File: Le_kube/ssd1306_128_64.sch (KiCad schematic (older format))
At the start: 15 parts

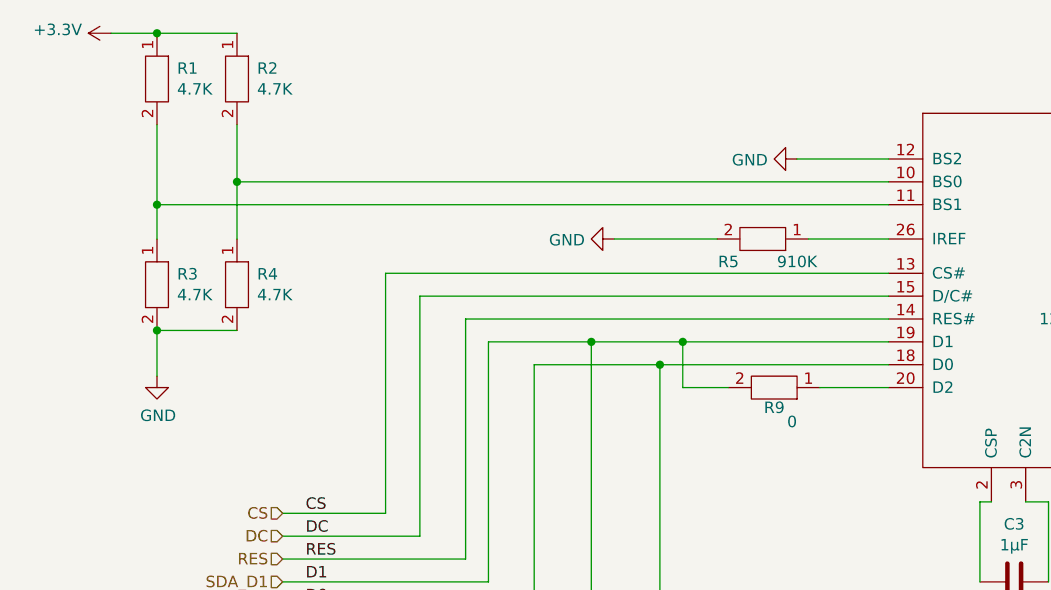
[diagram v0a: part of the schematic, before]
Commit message: merge screen + temp sensor CAO
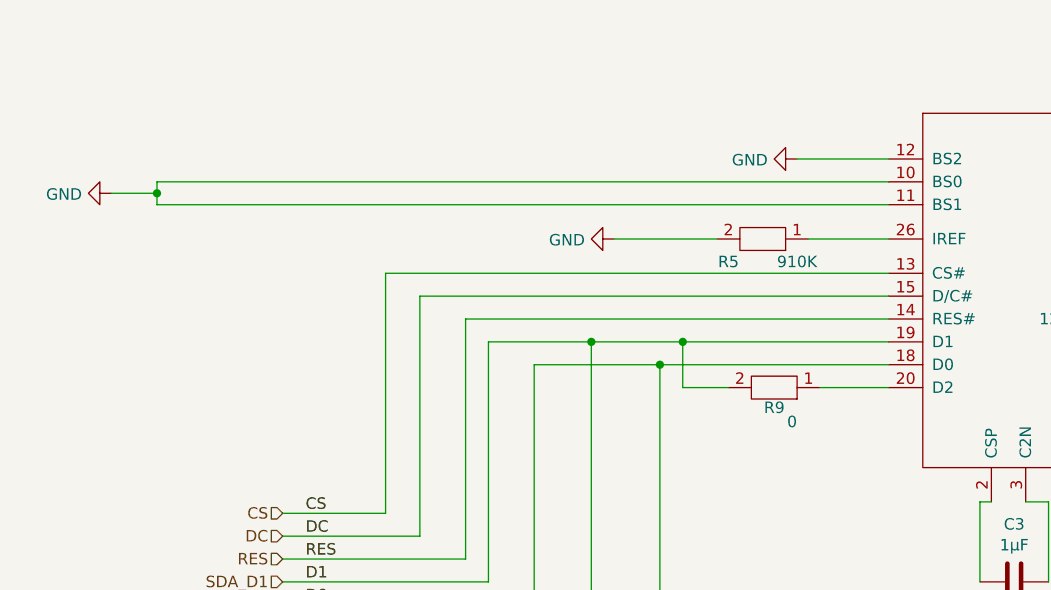
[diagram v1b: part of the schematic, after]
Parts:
- removed R1, R2, R3, R4: 4.7K, symbol Kube_library:R
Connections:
- net GND: now also U.10 (BS0), U.11 (BS1)
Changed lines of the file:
@@
 Comment4 ""
 $EndDescr
-$Comp
-L Kube_library:R R1
-U 1 1 606D3DEF
-P 2400 1350
-F 0 "R1" V 2354 1438 50  0000 L CNN
-F 1 "4.7K" V 2445 1438 50  0000 L CNN
-F 2 "" H 2400 1350 50  0001 C CNN
-F 3 "" H 2400 1350 50  0001 C CNN
-	1    2400 1350
-	0    1    1    0
-$EndComp
-$Comp
-L Kube_library:R R2
-U 1 1 606D4491
-P 2750 1350
-F 0 "R2" V 2704 1438 50  0000 L CNN
-F 1 "4.7K" V 2795 1438 50  0000 L CNN
-F 2 "" H 2750 1350 50  0001 C CNN
-F 3 "" H 2750 1350 50  0001 C CNN
-	1    2750 1350
-	0    1    1    0
-$EndComp
-Wire Wire Line
-	2750 1150 2400 1150
-Connection ~ 2400 1150
-Wire Wire Line
-	2400 1150 2200 1150
-$Comp
-L Kube_library:R R4
-U 1 1 606D4D1A
-P 2750 2250
-F 0 "R4" V 2704 2338 50  0000 L CNN
-F 1 "4.7K" V 2795 2338 50  0000 L CNN
-F 2 "" H 2750 2250 50  0001 C CNN
-F 3 "" H 2750 2250 50  0001 C CNN
-	1    2750 2250
-	0    1    1    0
-$EndComp
-$Comp
-L Kube_library:R R3
-U 1 1 606D54AA
-P 2400 2250
-F 0 "R3" V 2354 2338 50  0000 L CNN
-F 1 "4.7K" V 2445 2338 50  0000 L CNN
-F 2 "" H 2400 2250 50  0001 C CNN
-F 3 "" H 2400 2250 50  0001 C CNN
-	1    2400 2250
-	0    1    1    0
-$EndComp
-Wire Wire Line
-	2400 1550 2400 1900
-Wire Wire Line
-	2750 1550 2750 1800
-Connection ~ 2400 1900
-Wire Wire Line
-	2400 1900 2400 2050
-Connection ~ 2750 1800
-Wire Wire Line
-	2750 1800 2750 2050
-Wire Wire Line
-	2400 2450 2750 2450
-Wire Wire Line
-	2400 2450 2400 2650
-Connection ~ 2400 2450
-$Comp
-L power:GND #PWR?
-U 1 1 606D6329
-P 2400 2650
-F 0 "#PWR?" H 2400 2400 50  0001 C CNN
-F 1 "GND" H 2405 2477 50  0000 C CNN
-F 2 "" H 2400 2650 50  0001 C CNN
-F 3 "" H 2400 2650 50  0001 C CNN
-	1    2400 2650
-	1    0    0    -1
-$EndComp
 Wire Wire Line
 	5600 1700 5200 1700
@@
 	4700 2700 4700 2500
 Connection ~ 4700 2500
-Wire Wire Line
-	2750 1800 5600 1800
 Wire Wire Line
 	2400 1900 5600 1900
@@
 Wire Wire Line
 	6700 3200 6800 3200
-$Comp
-L power:+3.3V #PWR?
-U 1 1 607E436B
-P 2200 1150
-F 0 "#PWR?" H 2200 1000 50  0001 C CNN
-F 1 "+3.3V" V 2215 1278 50  0000 L CNN
-F 2 "" H 2200 1150 50  0001 C CNN
-F 3 "" H 2200 1150 50  0001 C CNN
-	1    2200 1150
-	0    -1   -1   0
-$EndComp
 Text HLabel 2950 3250 0    50   Input ~ 0
 CS
@@
 Wire Wire Line
 	4450 4000 4450 5200
+Wire Wire Line
+	2400 1800 2400 1850
+Wire Wire Line
+	2400 1800 5600 1800
+Wire Wire Line
+	2400 1850 2200 1850
+Connection ~ 2400 1850
+Wire Wire Line
+	2400 1850 2400 1900
+$Comp
+L power:GND #PWR?
+U 1 1 606D33F3
+P 2200 1850
+F 0 "#PWR?" H 2200 1600 50  0001 C CNN
+F 1 "GND" V 2205 1722 50  0000 R CNN
+F 2 "" H 2200 1850 50  0001 C CNN
+F 3 "" H 2200 1850 50  0001 C CNN
+	1    2200 1850
+	0    1    1    0
+$EndComp
 $EndSCHEMATC

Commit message: sheet finish ?
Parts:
- renumbered C5 to C10, C6 to C11, C1 to C12, C2 to C13, C3 to C8, C4 to C9, R5 to R10, R9 to R11, R6 to R8, R7 to R9
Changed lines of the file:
@@
 $Descr A4 11693 8268
 encoding utf-8
-Sheet 3 4
+Sheet 3 5
 Title ""
 Date ""
@@
 $EndComp
 $Comp
-L Kube_library:R R5
+L Kube_library:R R10
 U 1 1 606D72A6
 P 5050 2050
-F 0 "R5" H 5200 2150 50  0000 C CNN
+F 0 "R10" H 5200 2150 50  0000 C CNN
 F 1 "910K" H 4900 2150 50  0000 C CNN
 F 2 "" H 5050 2050 50  0001 C CNN
@@
 	8250 2400 8250 2500
 $Comp
-L Kube_library:C C3
+L Kube_library:C C8
 U 1 1 606B34DF
 P 6150 3550
-F 0 "C3" H 6150 3802 50  0000 C CNN
+F 0 "C8" H 6150 3802 50  0000 C CNN
 F 1 "1µF" H 6150 3711 50  0000 C CNN
 F 2 "" V 6300 3588 50  0001 C CNN
@@
 	6300 3550 6300 3200
 $Comp
-L Kube_library:C C4
+L Kube_library:C C9
 U 1 1 606BB097
 P 6650 3550
-F 0 "C4" H 6650 3802 50  0000 C CNN
+F 0 "C9" H 6650 3802 50  0000 C CNN
 F 1 "1µF" H 6650 3711 50  0000 C CNN
 F 2 "" V 6800 3588 50  0001 C CNN
@@
 	6800 3550 6800 3200
 $Comp
-L Kube_library:C C5
+L Kube_library:C C10
 U 1 1 606BD997
 P 7050 3450
-F 0 "C5" V 7150 3600 50  0000 R CNN
+F 0 "C10" V 7150 3600 50  0000 R CNN
 F 1 "4.7µF" V 6950 3650 50  0000 R CNN
 F 2 "" V 7200 3488 50  0001 C CNN
@@
 $EndComp
 $Comp
-L Kube_library:C C6
+L Kube_library:C C11
 U 1 1 606C0222
 P 7250 3450
-F 0 "C6" V 7350 3600 50  0000 R CNN
+F 0 "C11" V 7350 3600 50  0000 R CNN
 F 1 "2.2µF" V 7150 3400 50  0000 R CNN
 F 2 "" V 7400 3488 50  0001 C CNN
@@
 	5600 2700 5300 2700
 $Comp
-L Kube_library:R R9
+L Kube_library:R R11
 U 1 1 60712FDF
 P 5100 2700
-F 0 "R9" H 5054 2788 50  0000 L CNN
+F 0 "R11" H 5054 2788 50  0000 L CNN
 F 1 "0" H 5000 2850 50  0000 L CNN
 F 2 "" H 5100 2700 50  0001 C CNN
@@
 $EndComp
 $Comp
-L Kube_library:C C1
+L Kube_library:C C12
 U 1 1 6076456A
 P 8900 2800
-F 0 "C1" V 8854 2915 50  0000 L CNN
+F 0 "C12" V 8854 2915 50  0000 L CNN
 F 1 "1µF" V 8945 2915 50  0000 L CNN
 F 2 "" V 9050 2838 50  0001 C CNN
@@
 	8500 2650 8900 2650
 $Comp
-L Kube_library:C C2
+L Kube_library:C C13
 U 1 1 6076CFA7
 P 9300 2800
-F 0 "C2" V 9254 2915 50  0000 L CNN
+F 0 "C13" V 9254 2915 50  0000 L CNN
 F 1 "1µF" V 9345 2915 50  0000 L CNN
 F 2 "" V 9450 2838 50  0001 C CNN
@@
 	4600 3600 4600 2600
 $Comp
-L Kube_library:R R7
+L Kube_library:R R9
 U 1 1 606DE359
 P 4600 3800
-F 0 "R7" V 4554 3888 50  0000 L CNN
+F 0 "R9" V 4554 3888 50  0000 L CNN
 F 1 "4.7K" V 4645 3888 50  0000 L CNN
 F 2 "" H 4600 3800 50  0001 C CNN
@@
 $EndComp
 $Comp
-L Kube_library:R R6
+L Kube_library:R R8
 U 1 1 606DDDC0
 P 4300 3800
-F 0 "R6" V 4254 3888 50  0000 L CNN
+F 0 "R8" V 4254 3888 50  0000 L CNN
 F 1 "4.7K" V 4345 3888 50  0000 L CNN
 F 2 "" H 4300 3800 50  0001 C CNN

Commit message: fin de la schematic
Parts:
- renumbered U to U2
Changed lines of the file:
@@
 	5600 1700 5200 1700
 $Comp
-L power:GND #PWR?
+L power:GND #PWR0123
 U 1 1 606D7059
 P 5200 1700
-F 0 "#PWR?" H 5200 1450 50  0001 C CNN
+F 0 "#PWR0123" H 5200 1450 50  0001 C CNN
 F 1 "GND" V 5205 1572 50  0000 R CNN
 F 2 "" H 5200 1700 50  0001 C CNN
@@
 	4400 2050 4850 2050
 $Comp
-L power:GND #PWR?
+L power:GND #PWR0124
 U 1 1 606D94A8
 P 4400 2050
-F 0 "#PWR?" H 4400 1800 50  0001 C CNN
+F 0 "#PWR0124" H 4400 1800 50  0001 C CNN
 F 1 "GND" V 4405 1922 50  0000 R CNN
 F 2 "" H 4400 2050 50  0001 C CNN
@@
 NoConn ~ 8100 1700
 $Comp
-L power:GND #PWR?
+L power:GND #PWR0125
 U 1 1 606DA2EF
 P 8250 2500
-F 0 "#PWR?" H 8250 2250 50  0001 C CNN
+F 0 "#PWR0125" H 8250 2250 50  0001 C CNN
 F 1 "GND" H 8400 2400 50  0000 C CNN
 F 2 "" H 8250 2500 50  0001 C CNN
@@
 	7050 3600 7050 3750
 $Comp
-L power:GND #PWR?
+L power:GND #PWR0126
 U 1 1 606C45C5
 P 7050 3800
-F 0 "#PWR?" H 7050 3550 50  0001 C CNN
+F 0 "#PWR0126" H 7050 3550 50  0001 C CNN
 F 1 "GND" H 7055 3627 50  0000 C CNN
 F 2 "" H 7050 3800 50  0001 C CNN
@@
 	8500 2950 8500 3050
 $Comp
-L power:GND #PWR?
+L power:GND #PWR0127
 U 1 1 6075A80C
 P 8500 3050
-F 0 "#PWR?" H 8500 2800 50  0001 C CNN
+F 0 "#PWR0127" H 8500 2800 50  0001 C CNN
 F 1 "GND" H 8505 2877 50  0000 C CNN
 F 2 "" H 8500 3050 50  0001 C CNN
@@
 	7900 1900 8250 1900
 $Comp
-L Kube_library:128x64_OLED U
+L Kube_library:128x64_OLED U2
 U 1 1 606CAE59
 P 6750 2500
-F 0 "U" H 6500 2500 50  0000 C CNN
+F 0 "U2" H 6500 2500 50  0000 C CNN
 F 1 "128x64_OLED" H 6500 2600 50  0000 C CNN
 F 2 "" H 6750 2500 50  0001 C CNN
@@
 SCK_D0
 $Comp
-L power:+3.3V #PWR?
+L power:+3.3V #PWR0128
 U 1 1 607F2FDD
 P 9300 2650
-F 0 "#PWR?" H 9300 2500 50  0001 C CNN
+F 0 "#PWR0128" H 9300 2500 50  0001 C CNN
 F 1 "+3.3V" V 9315 2778 50  0000 L CNN
 F 2 "" H 9300 2650 50  0001 C CNN
@@
 	4450 4000 4600 4000
 $Comp
-L power:+3.3V #PWR?
+L power:+3.3V #PWR0129
 U 1 1 6080D5DA
 P 4450 5200
-F 0 "#PWR?" H 4450 5050 50  0001 C CNN
+F 0 "#PWR0129" H 4450 5050 50  0001 C CNN
 F 1 "+3.3V" H 4465 5373 50  0000 C CNN
 F 2 "" H 4450 5200 50  0001 C CNN
@@
 	2400 1850 2400 1900
 $Comp
-L power:GND #PWR?
+L power:GND #PWR0130
 U 1 1 606D33F3
 P 2200 1850
-F 0 "#PWR?" H 2200 1600 50  0001 C CNN
+F 0 "#PWR0130" H 2200 1600 50  0001 C CNN
 F 1 "GND" V 2205 1722 50  0000 R CNN
 F 2 "" H 2200 1850 50  0001 C CNN

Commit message: connector jack DC add
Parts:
- C10, C11, C12, C13, C8, C9: symbol Kube_library:C -> Le_kube-rescue:C-Kube_library
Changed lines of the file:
@@
 	8250 2400 8250 2500
 $Comp
-L Kube_library:C C8
+L Le_kube-rescue:C-Kube_library C8
 U 1 1 606B34DF
 P 6150 3550
+AR Path="/606B34DF" Ref="C8"  Part="1"
+AR Path="/60669017/606B34DF" Ref="C8"  Part="1"
 F 0 "C8" H 6150 3802 50  0000 C CNN
 F 1 "1µF" H 6150 3711 50  0000 C CNN
@@
 	6300 3550 6300 3200
 $Comp
-L Kube_library:C C9
+L Le_kube-rescue:C-Kube_library C9
 U 1 1 606BB097
 P 6650 3550
+AR Path="/606BB097" Ref="C9"  Part="1"
+AR Path="/60669017/606BB097" Ref="C9"  Part="1"
 F 0 "C9" H 6650 3802 50  0000 C CNN
 F 1 "1µF" H 6650 3711 50  0000 C CNN
@@
 	6800 3550 6800 3200
 $Comp
-L Kube_library:C C10
+L Le_kube-rescue:C-Kube_library C10
 U 1 1 606BD997
 P 7050 3450
+AR Path="/606BD997" Ref="C10"  Part="1"
+AR Path="/60669017/606BD997" Ref="C10"  Part="1"
 F 0 "C10" V 7150 3600 50  0000 R CNN
 F 1 "4.7µF" V 6950 3650 50  0000 R CNN
@@
 $EndComp
 $Comp
-L Kube_library:C C11
+L Le_kube-rescue:C-Kube_library C11
 U 1 1 606C0222
 P 7250 3450
+AR Path="/606C0222" Ref="C11"  Part="1"
+AR Path="/60669017/606C0222" Ref="C11"  Part="1"
 F 0 "C11" V 7350 3600 50  0000 R CNN
 F 1 "2.2µF" V 7150 3400 50  0000 R CNN
@@
 $EndComp
 $Comp
-L Kube_library:C C12
+L Le_kube-rescue:C-Kube_library C12
 U 1 1 6076456A
 P 8900 2800
+AR Path="/6076456A" Ref="C12"  Part="1"
+AR Path="/60669017/6076456A" Ref="C12"  Part="1"
 F 0 "C12" V 8854 2915 50  0000 L CNN
 F 1 "1µF" V 8945 2915 50  0000 L CNN
@@
 	8500 2650 8900 2650
 $Comp
-L Kube_library:C C13
+L Le_kube-rescue:C-Kube_library C13
 U 1 1 6076CFA7
 P 9300 2800
+AR Path="/6076CFA7" Ref="C13"  Part="1"
+AR Path="/60669017/6076CFA7" Ref="C13"  Part="1"
 F 0 "C13" V 9254 2915 50  0000 L CNN
 F 1 "1µF" V 9345 2915 50  0000 L CNN

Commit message: corrections
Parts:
- removed R11: 0, symbol Kube_library:R
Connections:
- net SDA_D1: now also U2.20 (D2)
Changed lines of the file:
@@
 	4050 3650 4050 2600
-Wire Wire Line
-	5600 2700 5300 2700
-$Comp
-L Kube_library:R R11
-U 1 1 60712FDF
-P 5100 2700
-F 0 "R11" H 5054 2788 50  0000 L CNN
-F 1 "0" H 5000 2850 50  0000 L CNN
-F 2 "" H 5100 2700 50  0001 C CNN
-F 3 "" H 5100 2700 50  0001 C CNN
-	1    5100 2700
-	-1   0    0    1
-$EndComp
-Wire Wire Line
-	4900 2700 4700 2700
 Wire Wire Line
 	4700 2700 4700 2500
@@
 	0    1    1    0
 $EndComp
+Wire Wire Line
+	4700 2700 5600 2700
 $EndSCHEMATC

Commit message: footprints done
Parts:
- C10, C11, C12, C13, C8, C9: footprint (none) -> Le_kube:C_0603_1608Metric_Pad1.08x0.95mm_HandSolder
- R10, R8, R9: footprint (none) -> Le_kube:R_0603_1608Metric_Pad0.98x0.95mm_HandSolder
- U2: footprint (none) -> Le_kube:OLED-0.96-12864
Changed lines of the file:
@@
 F 0 "R10" H 5200 2150 50  0000 C CNN
 F 1 "910K" H 4900 2150 50  0000 C CNN
-F 2 "" H 5050 2050 50  0001 C CNN
+F 2 "Le_kube:R_0603_1608Metric_Pad0.98x0.95mm_HandSolder" H 5050 2050 50  0001 C CNN
 F 3 "" H 5050 2050 50  0001 C CNN
 	1    5050 2050
@@
 F 0 "C8" H 6150 3802 50  0000 C CNN
 F 1 "1µF" H 6150 3711 50  0000 C CNN
-F 2 "" V 6300 3588 50  0001 C CNN
+F 2 "Le_kube:C_0603_1608Metric_Pad1.08x0.95mm_HandSolder" V 6300 3588 50  0001 C CNN
 F 3 "~" H 6150 3550 50  0001 C CNN
 	1    6150 3550
@@
 F 0 "C9" H 6650 3802 50  0000 C CNN
 F 1 "1µF" H 6650 3711 50  0000 C CNN
-F 2 "" V 6800 3588 50  0001 C CNN
+F 2 "Le_kube:C_0603_1608Metric_Pad1.08x0.95mm_HandSolder" V 6800 3588 50  0001 C CNN
 F 3 "~" H 6650 3550 50  0001 C CNN
 	1    6650 3550
@@
 F 0 "C10" V 7150 3600 50  0000 R CNN
 F 1 "4.7µF" V 6950 3650 50  0000 R CNN
-F 2 "" V 7200 3488 50  0001 C CNN
+F 2 "Le_kube:C_0603_1608Metric_Pad1.08x0.95mm_HandSolder" V 7200 3488 50  0001 C CNN
 F 3 "~" H 7050 3450 50  0001 C CNN
 	1    7050 3450
@@
 F 0 "C11" V 7350 3600 50  0000 R CNN
 F 1 "2.2µF" V 7150 3400 50  0000 R CNN
-F 2 "" V 7400 3488 50  0001 C CNN
+F 2 "Le_kube:C_0603_1608Metric_Pad1.08x0.95mm_HandSolder" V 7400 3488 50  0001 C CNN
 F 3 "~" H 7250 3450 50  0001 C CNN
 	1    7250 3450
@@
 F 0 "C12" V 8854 2915 50  0000 L CNN
 F 1 "1µF" V 8945 2915 50  0000 L CNN
-F 2 "" V 9050 2838 50  0001 C CNN
+F 2 "Le_kube:C_0603_1608Metric_Pad1.08x0.95mm_HandSolder" V 9050 2838 50  0001 C CNN
 F 3 "~" H 8900 2800 50  0001 C CNN
 	1    8900 2800
@@
 F 0 "C13" V 9254 2915 50  0000 L CNN
 F 1 "1µF" V 9345 2915 50  0000 L CNN
-F 2 "" V 9450 2838 50  0001 C CNN
+F 2 "Le_kube:C_0603_1608Metric_Pad1.08x0.95mm_HandSolder" V 9450 2838 50  0001 C CNN
 F 3 "~" H 9300 2800 50  0001 C CNN
 	1    9300 2800
@@
 F 0 "U2" H 6500 2500 50  0000 C CNN
 F 1 "128x64_OLED" H 6500 2600 50  0000 C CNN
-F 2 "" H 6750 2500 50  0001 C CNN
+F 2 "Le_kube:OLED-0.96-12864" H 6750 2500 50  0001 C CNN
 F 3 "~" H 6750 2500 50  0001 C CNN
 	1    6750 2500
@@
 F 0 "R9" V 4554 3888 50  0000 L CNN
 F 1 "4.7K" V 4645 3888 50  0000 L CNN
-F 2 "" H 4600 3800 50  0001 C CNN
+F 2 "Le_kube:R_0603_1608Metric_Pad0.98x0.95mm_HandSolder" H 4600 3800 50  0001 C CNN
 F 3 "" H 4600 3800 50  0001 C CNN
 	1    4600 3800
@@
 F 0 "R8" V 4254 3888 50  0000 L CNN
 F 1 "4.7K" V 4345 3888 50  0000 L CNN
-F 2 "" H 4300 3800 50  0001 C CNN
+F 2 "Le_kube:R_0603_1608Metric_Pad0.98x0.95mm_HandSolder" H 4300 3800 50  0001 C CNN
 F 3 "" H 4300 3800 50  0001 C CNN
 	1    4300 3800
